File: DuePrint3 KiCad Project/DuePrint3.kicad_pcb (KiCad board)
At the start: 2 copper layers, 208.9 x 75.2 mm, 50 parts, among them J1 430452412, J10 436500215, J11 M20-9990245, J12 M20-9990245, J13 EHT-125-01-S-D, J14 EHT-110-01-S-D, J15 EHT-125-01-S-D, J2 PPPC161LFBN-RC, J3 PPPC161LFBN-RC, J4 6P2C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

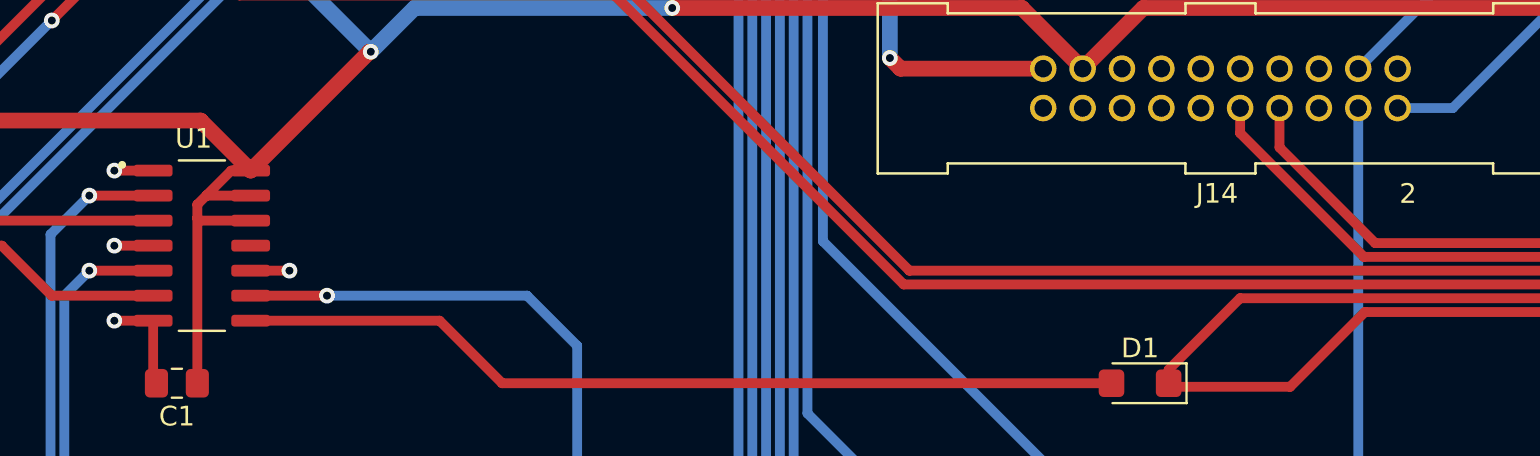
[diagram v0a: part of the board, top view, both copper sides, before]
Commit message: Footprint & Symbol reorg; PCB & Schematic now cleaned-up
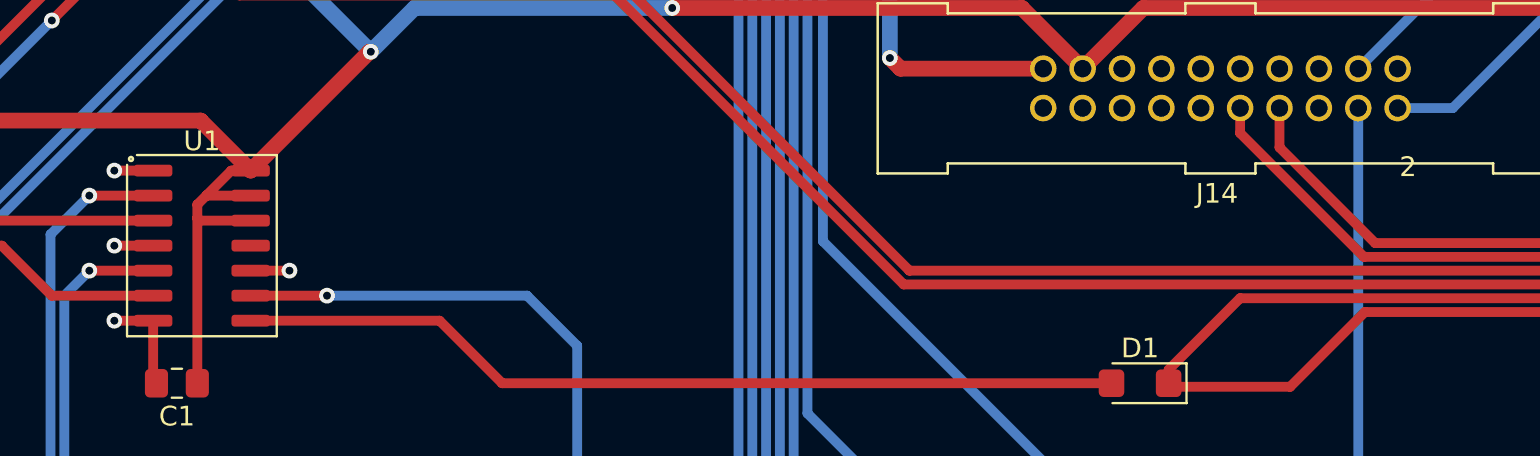
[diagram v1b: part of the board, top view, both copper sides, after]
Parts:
- D1: value 100v 1a -> 100v 1A
- J1: value 430452412 -> MF3.0-2x12-430452412
- J10, J7: value 436500215 -> MF3.0-1x2-436500215
- J11, J12: value M20-9990245 -> 2.54Header-1x2-M
- J13, J15: footprint EHT-125-01-S-D:SAMTEC_EHT-125-01-S-D -> DuePrint3-Lib:SAMTEC_EHT-125-01-S-D
- J14: footprint EHT-110-01-XX-D:EHT-110-01-XX-D -> DuePrint3-Lib:EHT-110-01-XX-D
- J2, J3: value PPPC161LFBN-RC -> 2.54Header-1x16-F
- J6: value M20-9990345 -> 2.54Header-1x3-M
- J8: value 436500815 -> MF3.0-1x8-436500815
- J9: value 430451812 -> MF3.0-2x9-430451812
- U1: footprint Stratasys Adapter:SOIC127P600X175-14N -> PCM_Package_SO_AKL:SOIC-14_3.9x8.7mm_P1.27mm
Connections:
- net Net-(J1-Pad15) renamed /T2 VSSA
- net Net-(J1-Pad16) renamed /T2
- net Net-(J1-Pad17) renamed /T1 VSSA
- net Net-(J1-Pad18) renamed /T1
- J1 pad 13: Net-(J1-Pad13) -> /T0
- J1 pad 14: Net-(J1-Pad14) -> /T0
- J15 pad 24: unconnected-(J15-Pad24) -> GND
- J15 pad 26: unconnected-(J15-Pad26) -> GND
- R3 pad 1: Net-(J1-Pad13) -> /T0
- R3 pad 2: Net-(J1-Pad14) -> /T0
- R6 pad 1: Net-(J1-Pad14) -> /T0
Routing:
- net /T0: track 0.00 -> 11.2 mm
- net Net-(J1-Pad14): track 7.54 -> 0.00 mm
- net Net-(J1-Pad13): track 3.67 -> 0.00 mm
